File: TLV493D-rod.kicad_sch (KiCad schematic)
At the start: 7 parts, among them CN1 AFC10-S04QCA-00, J1 Conn_01x04_Pin, U1 TLV493D

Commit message: fix incorrect footprint
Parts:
- U1: footprint Package_TO_SOT_SMD:SOT-23-6 -> TLV493D-rod:SOP-6_L3.0-W1.5-P0.95-LS2.5-BR
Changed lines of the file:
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@@
       (effects (font (size 1.27 1.27)) (justify left))
     )
-    (property "Footprint" "Package_TO_SOT_SMD:SOT-23-6" (at 146.05 116.84 0)
+    (property "Footprint" "TLV493D-rod:SOP-6_L3.0-W1.5-P0.95-LS2.5-BR" (at 146.05 116.84 0)
       (effects (font (size 1.27 1.27)) hide)
     )

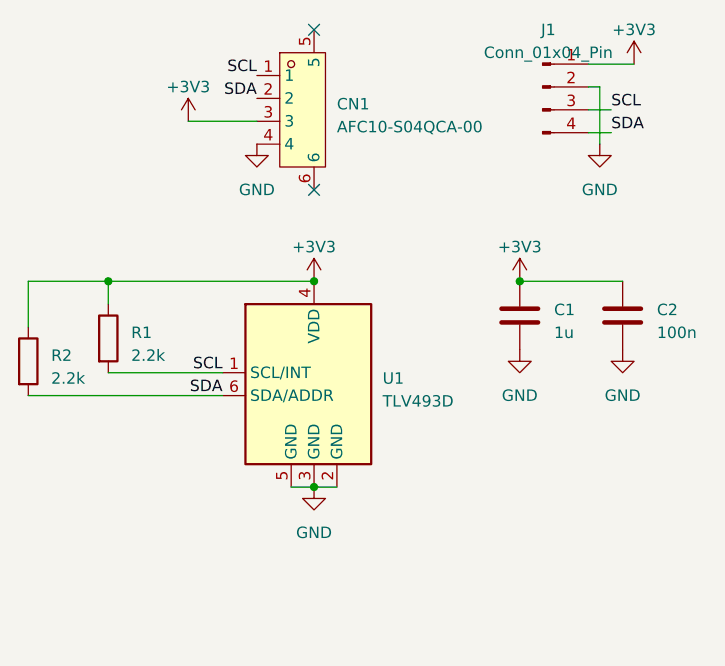
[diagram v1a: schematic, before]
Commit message: revamp mounting, fix qwiic pinout
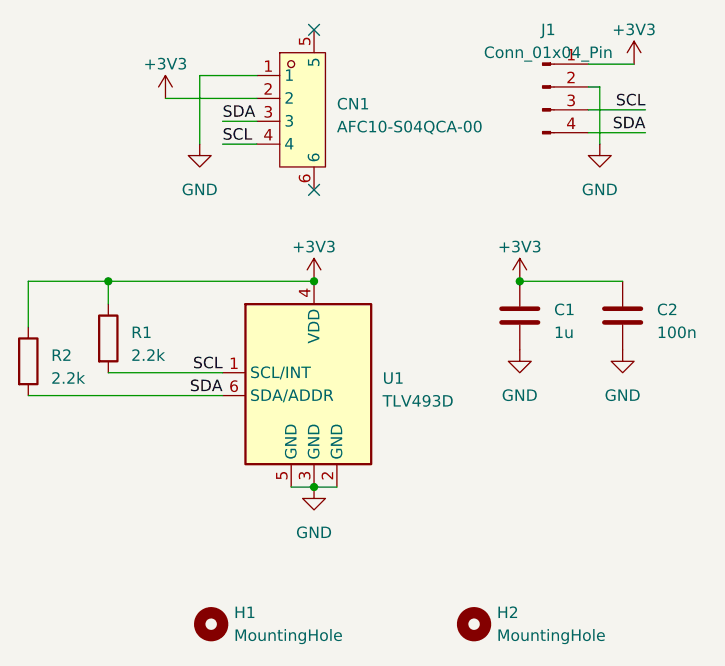
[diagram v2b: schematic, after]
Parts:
- added H1, H2: MountingHole, MountingHole:MountingHole_2.2mm_M2, symbol Mechanical:MountingHole
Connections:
- net +3V3: now also CN1.2; no longer CN1.3
- net GND: now also CN1.1; no longer CN1.4
- net SCL: now also CN1.4; no longer CN1.1
- net SDA: now also CN1.3; no longer CN1.2
